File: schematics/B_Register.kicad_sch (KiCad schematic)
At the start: 19 parts, among them U1 74LS173, U2 74LS173

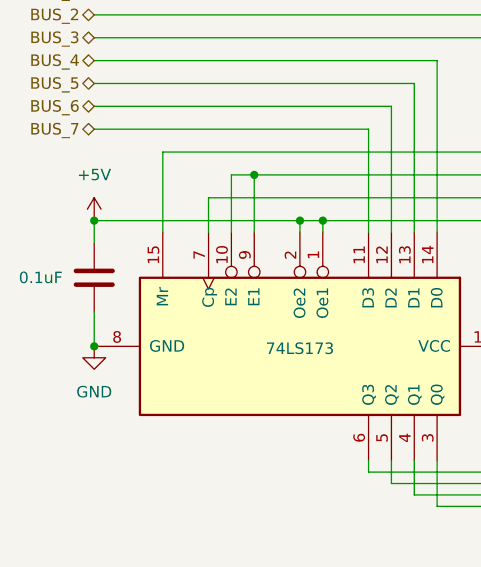
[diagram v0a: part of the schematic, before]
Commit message: feat: updated electrical diagrams & individual part list
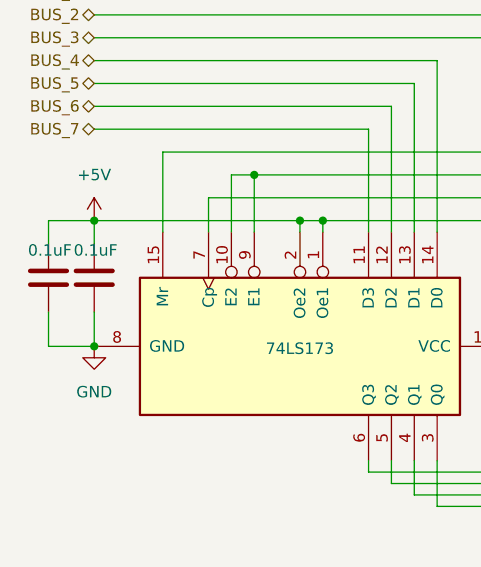
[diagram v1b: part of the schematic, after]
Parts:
- added C2: 0.1uF, symbol Device:C
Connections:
- net +5V: now also C2.1
- net GND: now also C2.2
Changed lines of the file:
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@@
+	(wire
+		(pts
+			(xy 102.87 85.09) (xy 107.95 85.09)
+		)
+		(stroke
+			(width 0)
+			(type default)
+		)
+	)
 	(wire
 		(pts
@@
 	(wire
 		(pts
+			(xy 102.87 87.63) (xy 102.87 85.09)
+		)
+		(stroke
+			(width 0)
+			(type default)
+		)
+	)
+	(wire
+		(pts
 			(xy 167.64 127) (xy 167.64 138.43)
 		)
@@
 	(wire
 		(pts
+			(xy 102.87 99.06) (xy 107.95 99.06)
+		)
+		(stroke
+			(width 0)
+			(type default)
+		)
+	)
+	(wire
+		(pts
 			(xy 171.45 153.67) (xy 175.26 153.67)
 		)
@@
 		(pts
 			(xy 187.96 62.23) (xy 187.96 86.36)
+		)
+		(stroke
+			(width 0)
+			(type default)
+		)
+	)
+	(wire
+		(pts
+			(xy 102.87 95.25) (xy 102.87 99.06)
 		)
 		(stroke
@@
 	)
 	(symbol
+		(lib_id "Device:C")
+		(at 102.87 91.44 0)
+		(unit 1)
+		(exclude_from_sim no)
+		(in_bom yes)
+		(on_board yes)
+		(dnp no)
+		(property "Reference" "C2"
+			(at 106.68 90.1699 0)
+			(effects
+				(font
+					(size 1.27 1.27)
+				)
+				(justify left)
+				(hide yes)
+			)
+		)
+		(property "Value" "0.1uF"
+			(at 100.584 88.392 0)
+			(effects
+				(font
+					(size 1.27 1.27)
+				)
+				(justify left)
+			)
+		)
+		(property "Footprint" ""
+			(at 103.8352 95.25 0)
+			(effects
+				(font
+					(size 1.27 1.27)
+				)
+				(hide yes)
+			)
+		)
+		(property "Datasheet" "~"
+			(at 102.87 91.44 0)
+			(effects
+				(font
+					(size 1.27 1.27)
+				)
+				(hide yes)
+			)
+		)
+		(property "Description" "Unpolarized capacitor"
+			(at 102.87 91.44 0)
+			(effects
+				(font
+					(size 1.27 1.27)
+				)
+				(hide yes)
+			)
+		)
+		(pin "2"
+		)
+		(pin "1"
+		)
+		(instances
+			(project "B_Register"
+				(path "/00881835-431f-440c-8b02-f05a8dfd3447"
+					(reference "C2")
+					(unit 1)
+				)
+			)
+		)
+	)
+	(symbol
 		(lib_id "74xx:74LS173")
 		(at 177.8 99.06 270)
@@
 		)
 		(property "Value" "0.1uF"
-			(at 99.568 91.44 0)
-			(effects
-				(font
+			(at 105.664 88.392 0)
+			(effects
+				(font
